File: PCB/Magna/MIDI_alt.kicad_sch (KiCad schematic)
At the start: 32 parts, among them J1001 DIN-5_180degree, J1002 DIN-5_180degree, J1003 DIN-5_180degree, U1001 74LVC2G14, U1002 74LVC2G14, U1003 74HC08D, U1004 TLP2361

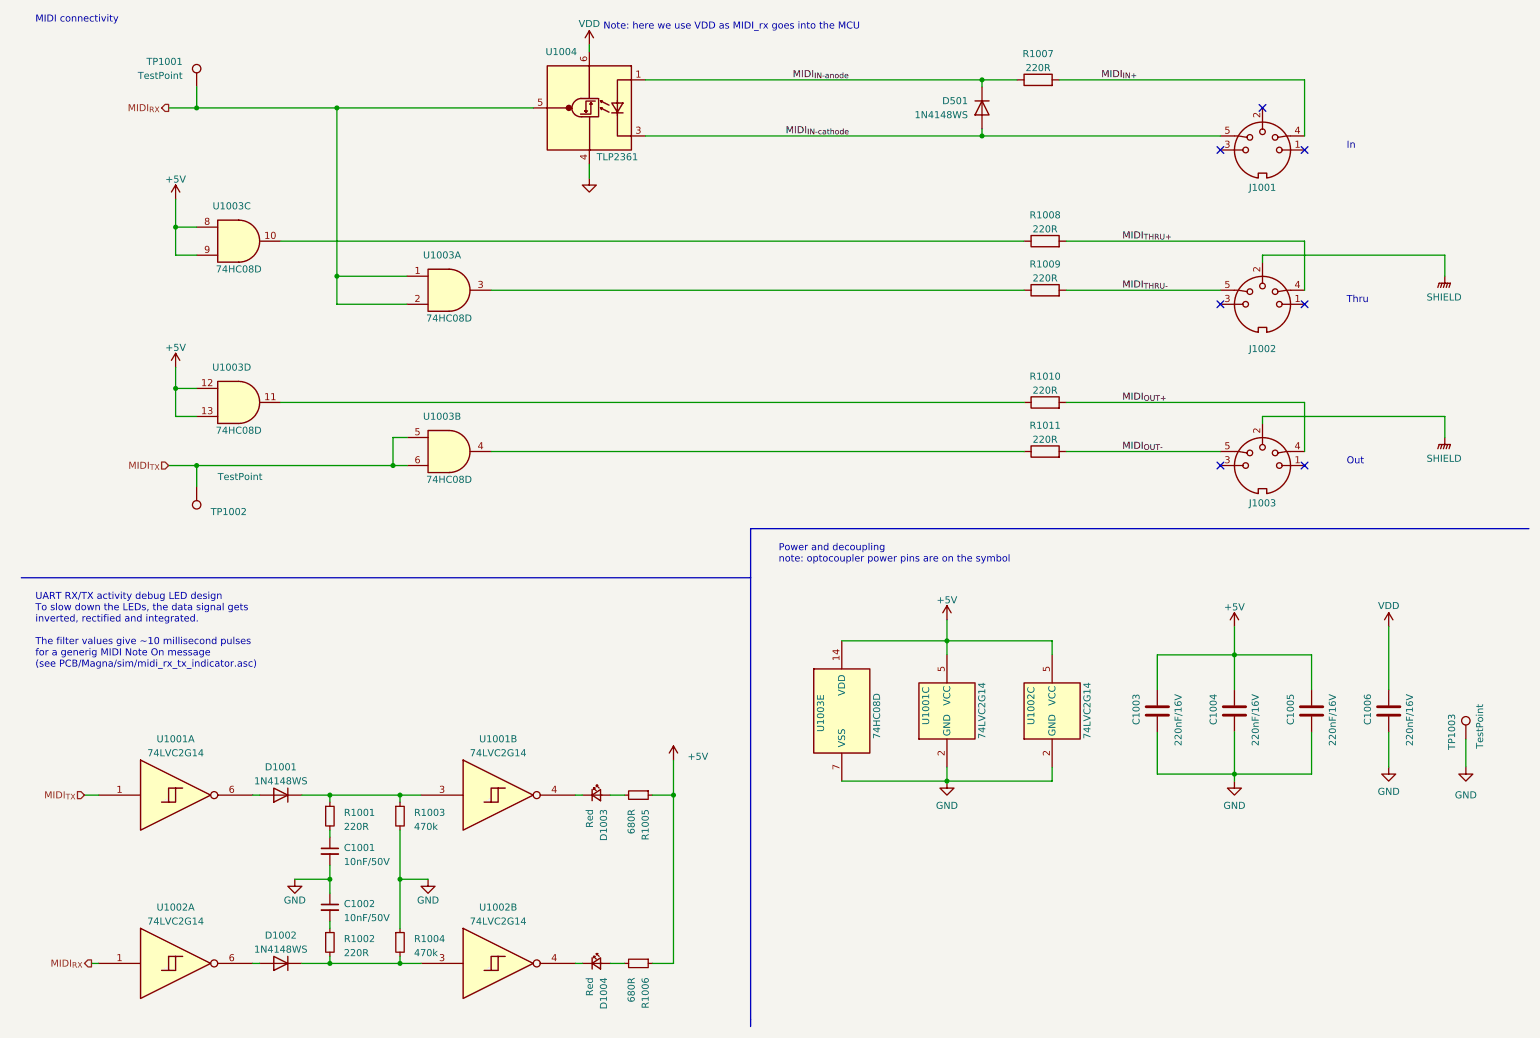
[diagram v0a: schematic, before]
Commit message: Mainboard layout (#19)
Also adds mounting holes to IO daughterboard
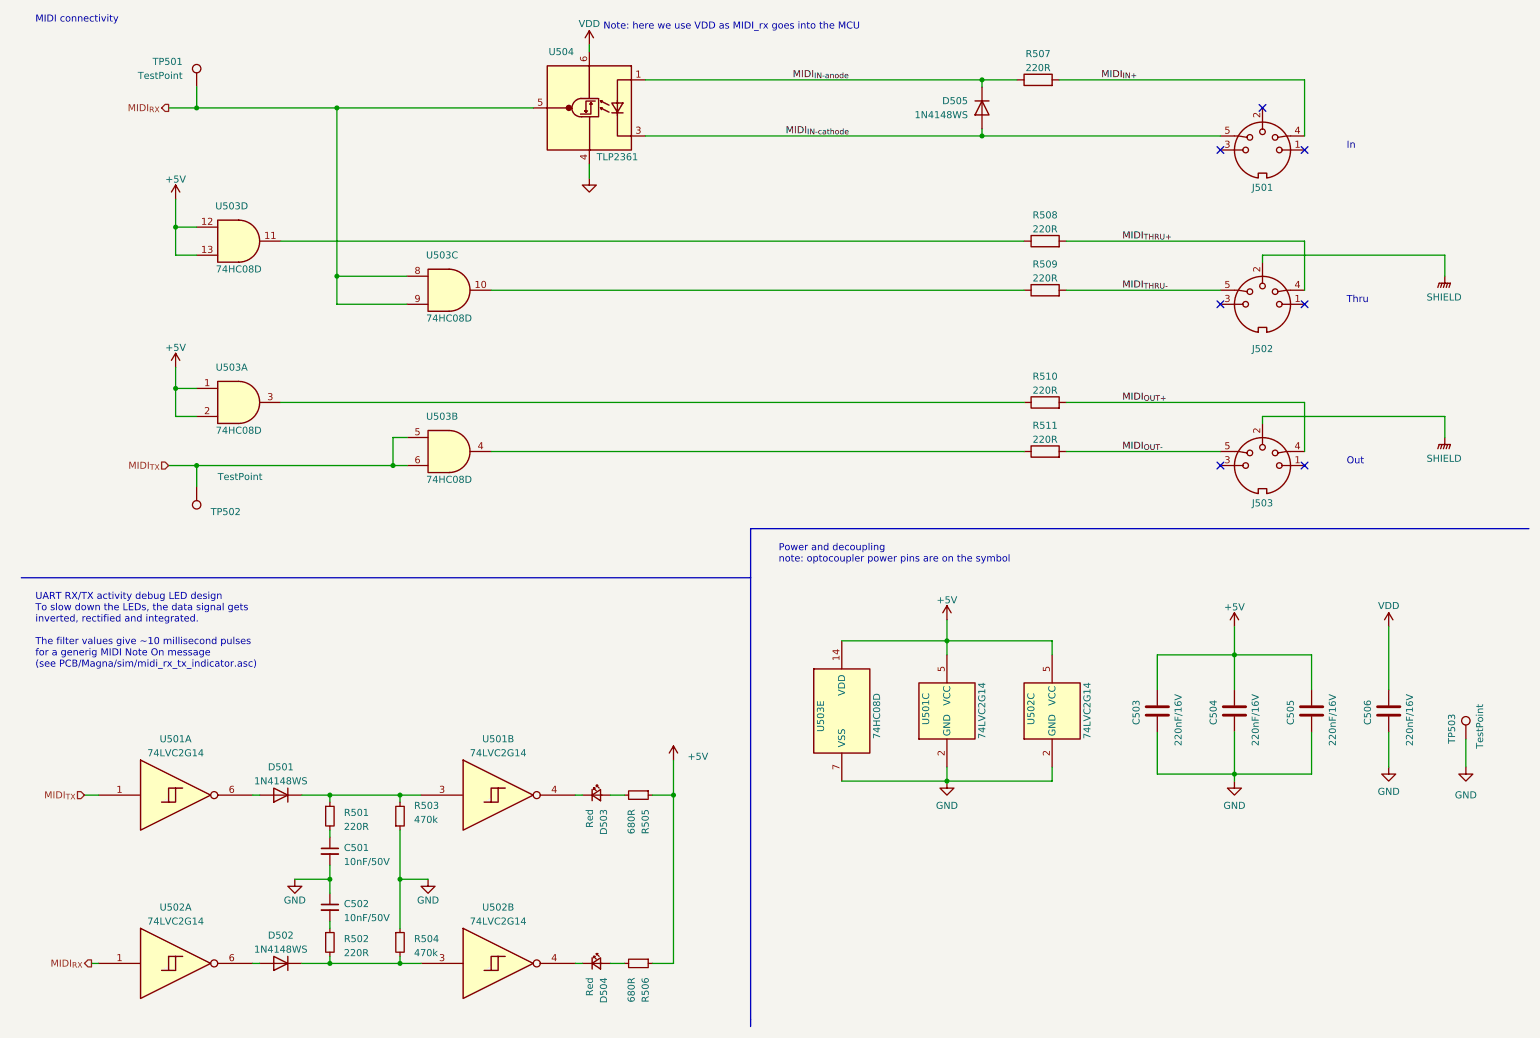
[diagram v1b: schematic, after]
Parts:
- renumbered C1001 to C501, C1002 to C502, C1003 to C503, C1004 to C504, C1005 to C505, C1006 to C506, D1001 to D501, D1002 to D502, D1003 to D503, D1004 to D504, D501 to D505, J1001 to J501, J1002 to J502, J1003 to J503, R1001 to R501, R1002 to R502, R1003 to R503, R1004 to R504, R1005 to R505, R1006 to R506, R1007 to R507, R1008 to R508, R1009 to R509, R1010 to R510, R1011 to R511, TP1001 to TP501, TP1002 to TP502, TP1003 to TP503, U1001 to U501, U1002 to U502, U1003 to U503, U1004 to U504
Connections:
- net +5V: now also U503.1, U503.2; no longer U503.8, U503.9
- net GND: now also R503.1; no longer R503.2
- net MIDI_{RX}: now also U503.8, U503.9; no longer U503.1, U503.2
- net at R510.1: now also U503.3; no longer U503.11
- net at D501.1 (K), R501.1, U501.3: now also R503.2; no longer R503.1
- net at R508.1: now also U503.11; no longer U503.10
- net at R509.1: now also U503.10; no longer U503.3
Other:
- moved on the sheet: U503A, U503C, U503D

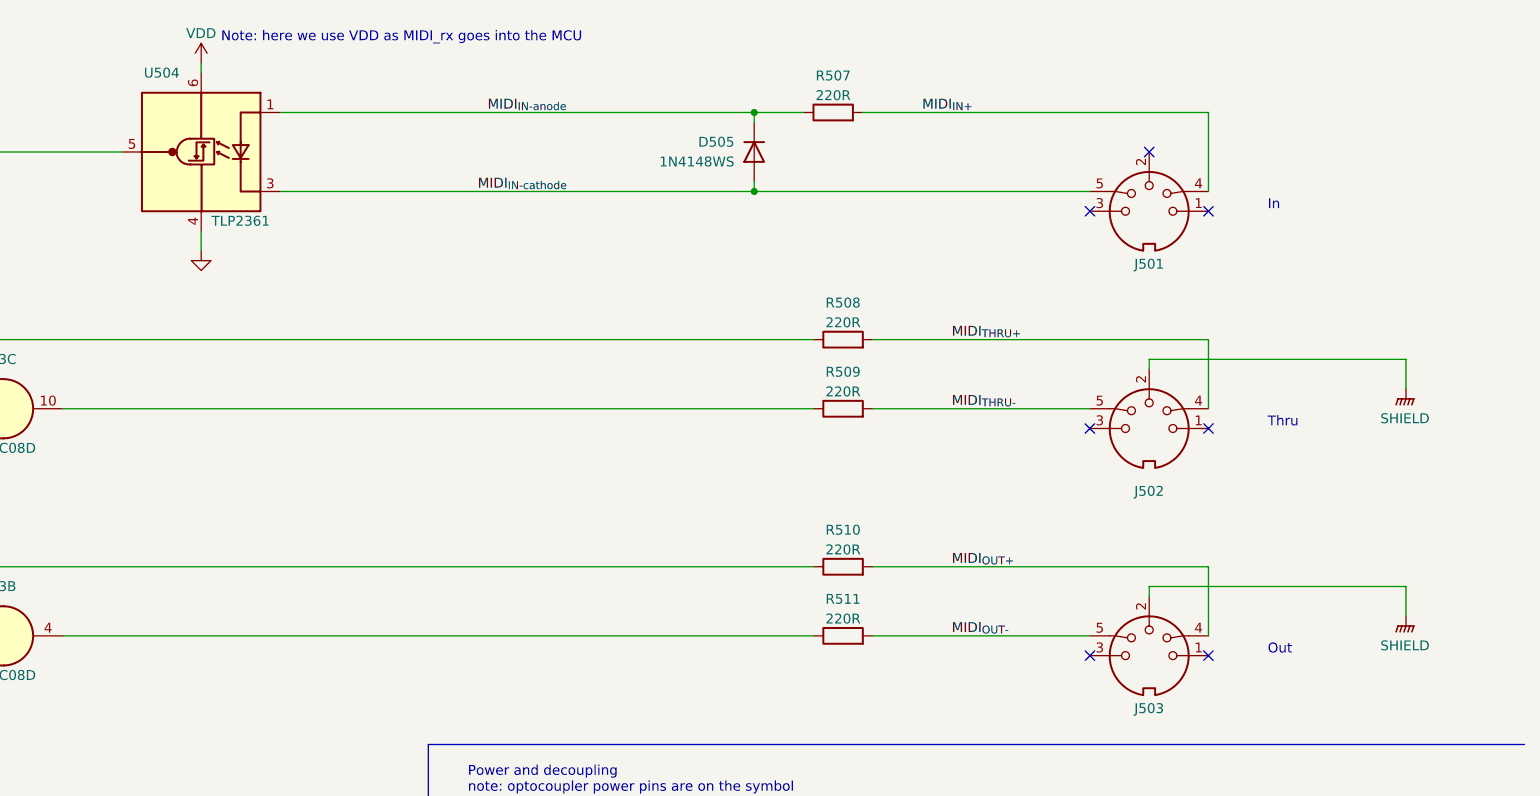
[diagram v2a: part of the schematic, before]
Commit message: Update Project to Kicad 8.0 and prepare for production
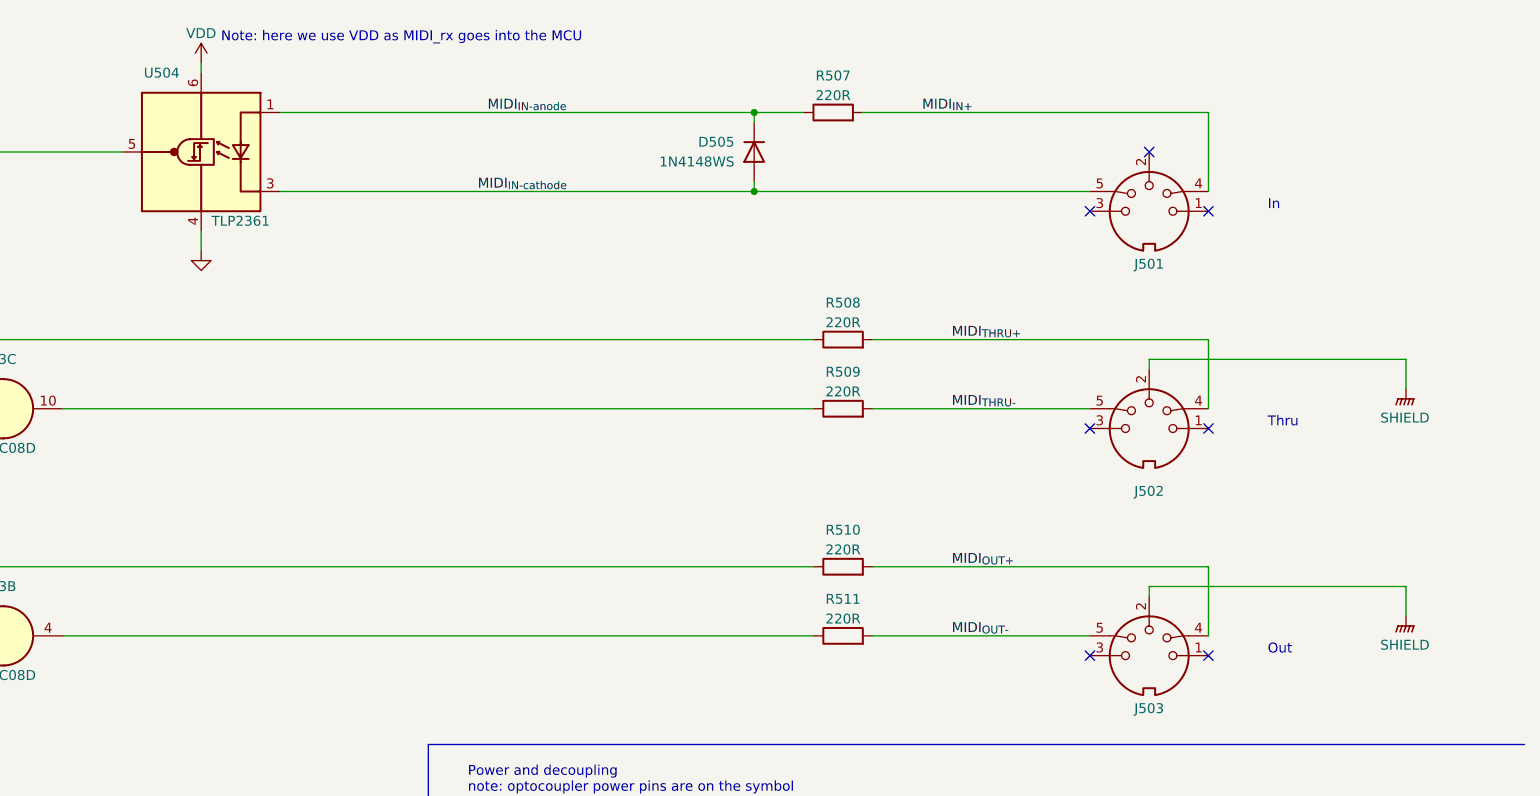
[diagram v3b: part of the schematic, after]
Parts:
- U501, U502: LCSC (none) -> C362110; LSCS C362110 -> (none)
- U504: LCSC (none) -> C107626; LSCS C107626 -> (none)

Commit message: Some updates to PCB
Honestly I cannot remember whats changed
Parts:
- C501, C502: LCSC C3908881 -> C1710
- R505, R506: LCSC C865612 -> C17798
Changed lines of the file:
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@@
 			)
 		)
-		(property "LCSC" "C865612"
+		(property "LCSC" "C17798"
 			(at 124.46 156.21 0)
 			(effects
@@
 			)
 		)
-		(property "LCSC" "C3908881"
+		(property "LCSC" "C1710"
 			(at 68.58 176.53 0)
 			(effects
@@
 			)
 		)
-		(property "LCSC" "C865612"
+		(property "LCSC" "C17798"
 			(at 124.46 186.69 0)
 			(effects
@@
 			)
 		)
-		(property "LCSC" "C3908881"
+		(property "LCSC" "C1710"
 			(at 68.58 166.37 0)
 			(effects
